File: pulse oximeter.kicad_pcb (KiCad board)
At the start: 2 copper layers, 43.5 x 22.6 mm, 28 parts, among them J1 USB_C_Receptacle_USB2.0_14P, J2 Conn_01x04_Socket, J3 Conn_01x02_Socket, Q1 FS8205A, SW1 SW_Push, SW2 RESET, U1 ATMEGA328P-AU, U2 AP2112K-3.3TRG1, U3 DW01A, U4 MAX30102EFD_, U5 MCP73831-2-OT, U6 CH340C, Y1 8MHz

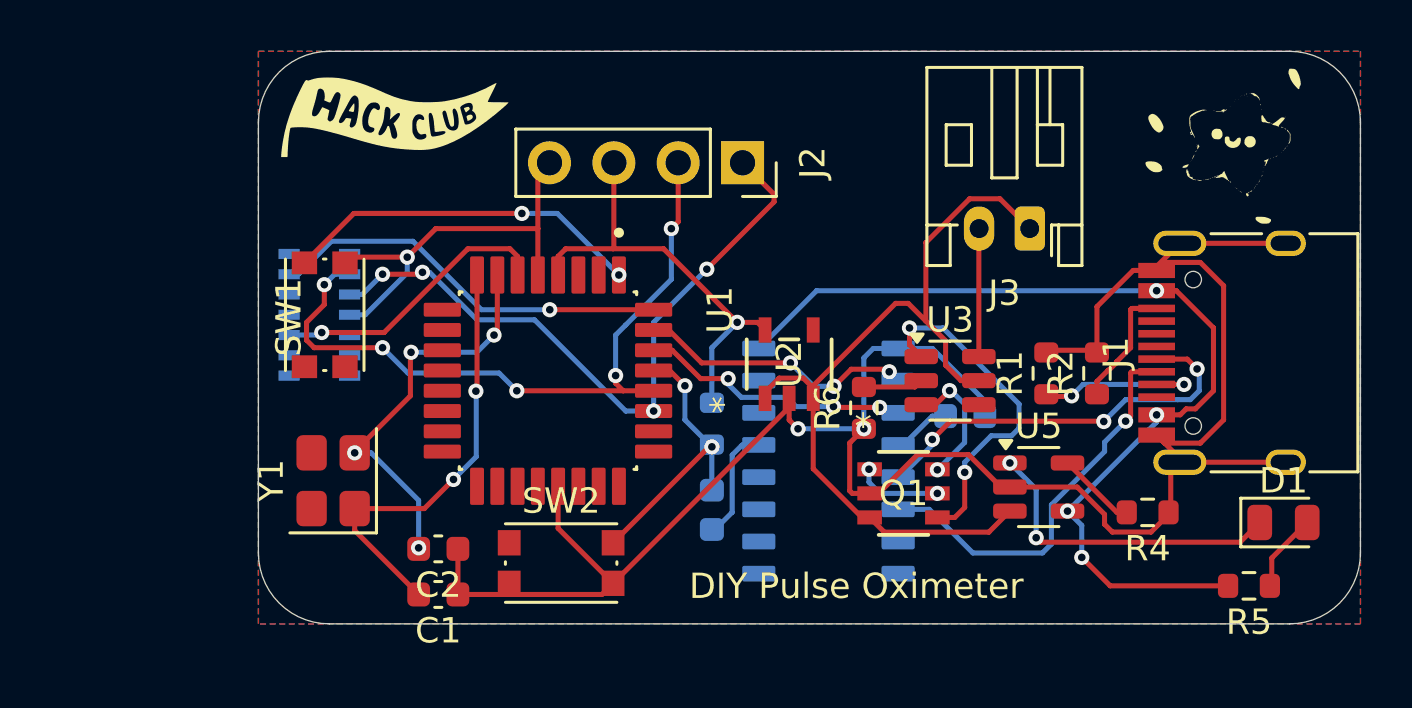
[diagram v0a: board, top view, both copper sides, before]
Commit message: Update pulse oximeter.kicad_pcb
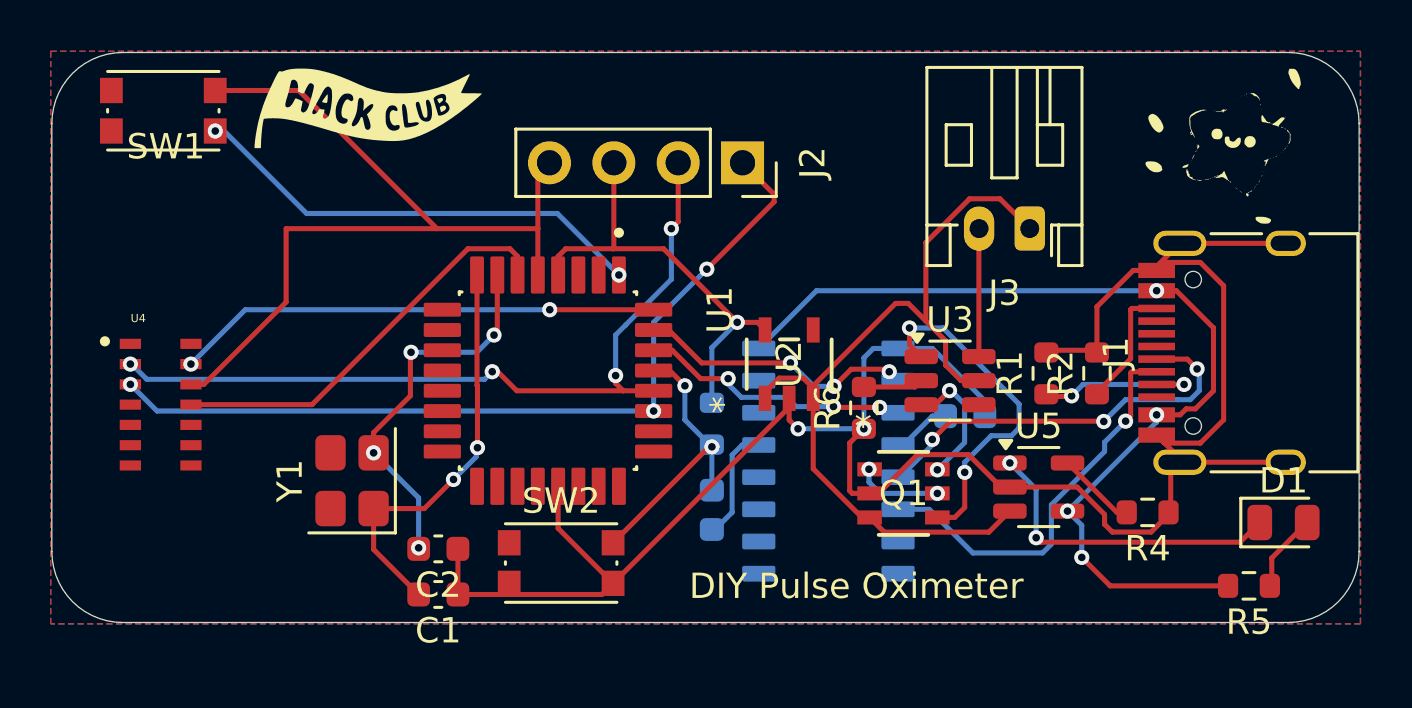
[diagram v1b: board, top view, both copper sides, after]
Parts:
- U4: moved to F.Cu
- moved SW1 10.3 mm to (128.5, 90.3), turned to 180 degrees
- moved U4 7.20 mm to (128.4, 101.9), turned to 0 degrees
- moved . 1.11 mm to (136.6, 90.2)
- moved Y1 0.75 mm to (135.9, 104.9)
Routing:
- net GND: track 102.0 -> 119.2 mm, vias 3 -> 2
- net SDA: track 26.9 -> 33.4 mm, vias 4 -> 3
- net +3.3V: track 28.6 -> 33.6 mm, vias 2 -> 1
- net Net-(U1-PD3): track 14.2 -> 18.3 mm
- net SCL: track 28.3 -> 31.5 mm, vias 5 -> 4
- net INT: track 16.0 -> 19.2 mm, vias 1 -> 2
- net Net-(U1-PB7): track 17.3 -> 16.3 mm
- net Net-(U1-PB6): track 16.4 -> 15.4 mm
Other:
- board size 43.5 x 22.6 mm -> 51.6 x 22.5 mm

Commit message: Edit PCB and Schematic
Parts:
- added C10: 4.7uF, Capacitor_SMD:C_0603_1608Metric, B.Cu at (131.7, 103.6)
- added C11: 100nF, Capacitor_SMD:C_0603_1608Metric, B.Cu at (132.1, 101.1)
- added C5: 100nF, Capacitor_SMD:C_0603_1608Metric, B.Cu at (163.4, 99.8)
- added C6: 100nF, Capacitor_SMD:C_0603_1608Metric, B.Cu at (141.6, 107.5)
- added C7: 100nF, Capacitor_SMD:C_0603_1608Metric, B.Cu at (143.3, 107.6)
- added C8: 1uF, Capacitor_SMD:C_0603_1608Metric, F.Cu at (153.2, 104.7)
- added C9: 4.7uF, Capacitor_SMD:C_0603_1608Metric, F.Cu at (153.1, 97.4)
- added R10: 1k ohm, Resistor_SMD:R_0603_1608Metric, B.Cu at (145.3, 99.9)
- added R11: 2k ohm, Resistor_SMD:R_0603_1608Metric, B.Cu at (143.6, 99.9)
- added R7: 100 ohm, Resistor_SMD:R_0603_1608Metric, F.Cu at (162.5, 98.2)
- added R8: 4.7k ohm, Resistor_SMD:R_0603_1608Metric, B.Cu at (142.6, 103.3)
- added R9: 4.7k ohm, Resistor_SMD:R_0603_1608Metric, B.Cu at (145.7, 103.3)
- moved SW1 0.40 mm to (128.5, 90.7)
- turned C4 to -90 degrees
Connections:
- C4 pad 2: RESET -> Net-(U6-~{DTR})
- Q1 pad 3: BVCC -> unconnected-(Q1-Pad3)
- Q1 pad 4: Net-(U3-OD) -> Net-(U3-OC)
- Q1 pad 5: Net-(Q1-Pad1) -> Net-(U3-OD)
- Q1 pad 6: Net-(U3-OC) -> Net-(Q1-Pad1)
- U1 pad 20: unconnected-(U1-AREF-Pad20) -> Net-(U1-AREF)
- U3 pad 5: BVCC -> Net-(U3-VCC)
- U6 pad 13: RESET -> Net-(U6-~{DTR})
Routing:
- net GND: track 119.2 -> 136.9 mm, vias 2 -> 7
- net +3.3V: track 33.6 -> 44.6 mm, vias 1 -> 5
- net Net-(U3-VCC): track 0.00 -> 6.63 mm, vias 0 -> 1
- net RXD: track 10.8 -> 16.2 mm, vias 3 -> 4
- net Net-(U6-~{DTR}): track 0.00 -> 4.62 mm
- net RESET: track 16.1 -> 11.5 mm
- net BVCC: track 33.5 -> 37.9 mm, vias 0 -> 2
- net SCL: track 31.5 -> 34.8 mm, vias 4 -> 5
- net TXD: track 11.0 -> 13.7 mm, vias 3 -> 4
- net BGND: track 5.06 -> 7.15 mm, vias 0 -> 1
- net Net-(U1-AREF): track 0.00 -> 1.68 mm, vias 0 -> 1
- net SDA: track 33.4 -> 34.7 mm
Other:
- board text added: "*"
